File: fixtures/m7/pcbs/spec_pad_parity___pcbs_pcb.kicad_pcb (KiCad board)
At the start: 2 copper layers, 1 part

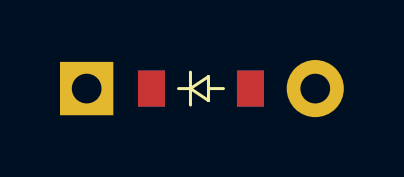
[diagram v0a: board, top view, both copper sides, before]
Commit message: Expand footprint specs and add JS footprints plan
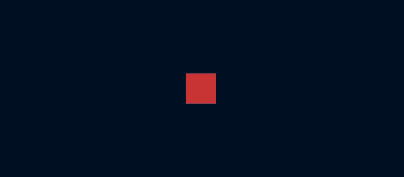
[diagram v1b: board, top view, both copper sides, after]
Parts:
- removed D1: , ComboDiode
- added PAD1: , SMDPad, F.Cu at (0.00, 0.00)
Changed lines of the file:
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@@
   )
   (net 0 "")
-(net 1 "D_FROM")
-(net 2 "D_TO")
+(net 1 "P1")
   (net_class Default "This is the default net class."
     (clearance 0.2)
@@
     (uvia_drill 0.1)
     (add_net "")
-(add_net "D_FROM")
-(add_net "D_TO")
+(add_net "P1")
   )
-        (module ComboDiode (layer F.Cu)
+        (module SMDPad (layer F.Cu)
             (at 0 0 0)
-            (fp_text reference "D1" (at 0 0) (layer F.SilkS) hide (effects (font (size 1.27 1.27) (thickness 0.15))))
+            (fp_text reference "PAD1" (at 0 0) (layer F.SilkS) hide (effects (font (size 1.27 1.27) (thickness 0.15))))
             (fp_text value "" (at 0 0) (layer F.SilkS) hide (effects (font (size 1.27 1.27) (thickness 0.15))))
-            (fp_line (start 0.25 0) (end 0.75 0) (layer F.SilkS) (width 0.1))
-            (fp_line (start 0.25 0.4) (end -0.35 0) (layer F.SilkS) (width 0.1))
-            (fp_line (start 0.25 -0.4) (end 0.25 0.4) (layer F.SilkS) (width 0.1))
-            (fp_line (start -0.35 0) (end 0.25 -0.4) (layer F.SilkS) (width 0.1))
-            (fp_line (start -0.35 0) (end -0.35 0.55) (layer F.SilkS) (width 0.1))
-            (fp_line (start -0.35 0) (end -0.35 -0.55) (layer F.SilkS) (width 0.1))
-            (fp_line (start -0.75 0) (end -0.35 0) (layer F.SilkS) (width 0.1))
-            (fp_line (start 0.25 0) (end 0.75 0) (layer B.SilkS) (width 0.1))
-            (fp_line (start 0.25 0.4) (end -0.35 0) (layer B.SilkS) (width 0.1))
-            (fp_line (start 0.25 -0.4) (end 0.25 0.4) (layer B.SilkS) (width 0.1))
-            (fp_line (start -0.35 0) (end 0.25 -0.4) (layer B.SilkS) (width 0.1))
-            (fp_line (start -0.35 0) (end -0.35 0.55) (layer B.SilkS) (width 0.1))
-            (fp_line (start -0.35 0) (end -0.35 -0.55) (layer B.SilkS) (width 0.1))
-            (fp_line (start -0.75 0) (end -0.35 0) (layer B.SilkS) (width 0.1))
-            (pad 1 smd rect (at -1.65 0 0) (size 0.9 1.2) (layers F.Cu F.Paste F.Mask) (net 2 "D_TO"))
-            (pad 2 smd rect (at 1.65 0 0) (size 0.9 1.2) (layers B.Cu B.Paste B.Mask) (net 1 "D_FROM"))
-            (pad 1 smd rect (at -1.65 0 0) (size 0.9 1.2) (layers B.Cu B.Paste B.Mask) (net 2 "D_TO"))
-            (pad 2 smd rect (at 1.65 0 0) (size 0.9 1.2) (layers F.Cu F.Paste F.Mask) (net 1 "D_FROM"))
-            (pad 1 thru_hole rect (at -3.81 0 0) (size 1.778 1.778) (drill 0.9906) (layers *.Cu *.Mask) (net 2 "D_TO"))
-            (pad 2 thru_hole circle (at 3.81 0 0) (size 1.905 1.905) (drill 0.9906) (layers *.Cu *.Mask) (net 1 "D_FROM"))
+            (pad 1 smd rect (at 0 0 0) (size 1 1) (layers F.Cu F.Paste F.Mask) (net 1 "P1"))
+            (pad 1 smd rect (at 0 0 0) (size 1 1) (layers B.Cu B.Paste B.Mask) (net 1 "P1"))
         )
 )
